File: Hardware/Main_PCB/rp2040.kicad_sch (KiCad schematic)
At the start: 27 parts, among them J3 Conn_02x18_Odd_Even, J4 Conn_02x18_Odd_Even, SW1 TL3342F160QG_TR, U3 RP2040, U3 W25Q128JVS, Y1 12Mhz

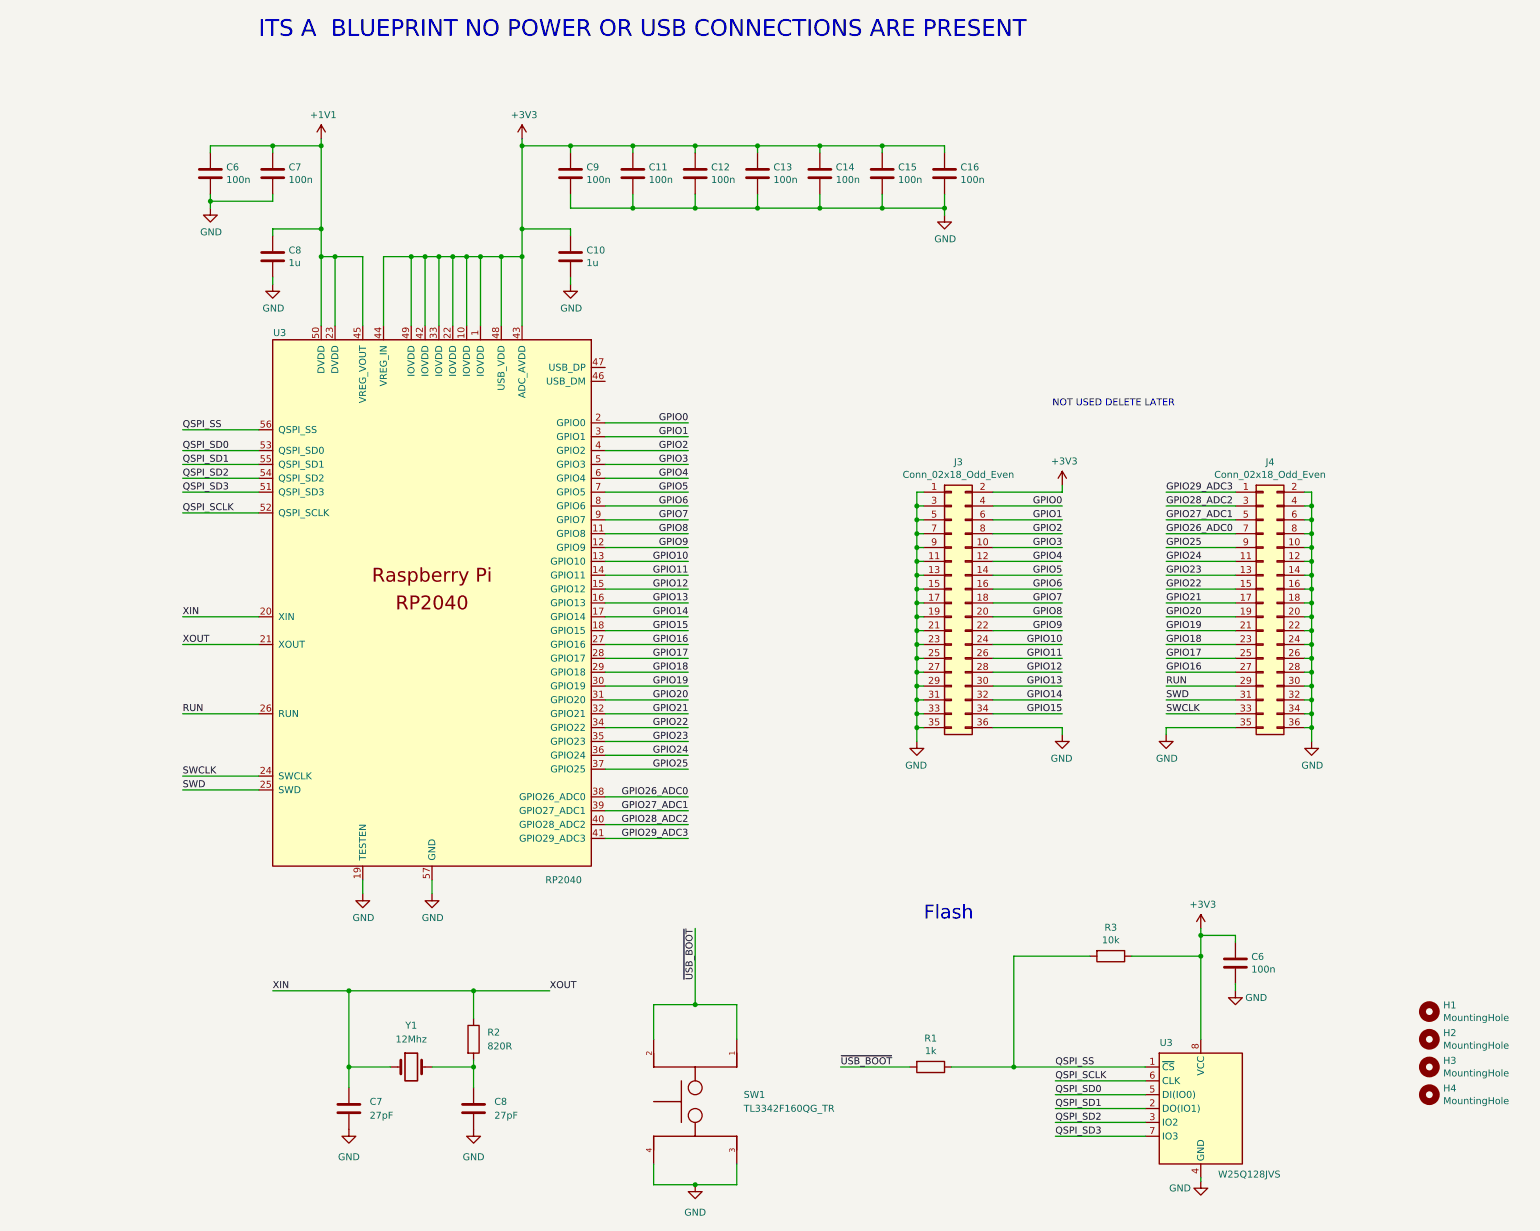
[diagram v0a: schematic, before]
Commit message: Trustworthy version of the MAIN PCB schematic
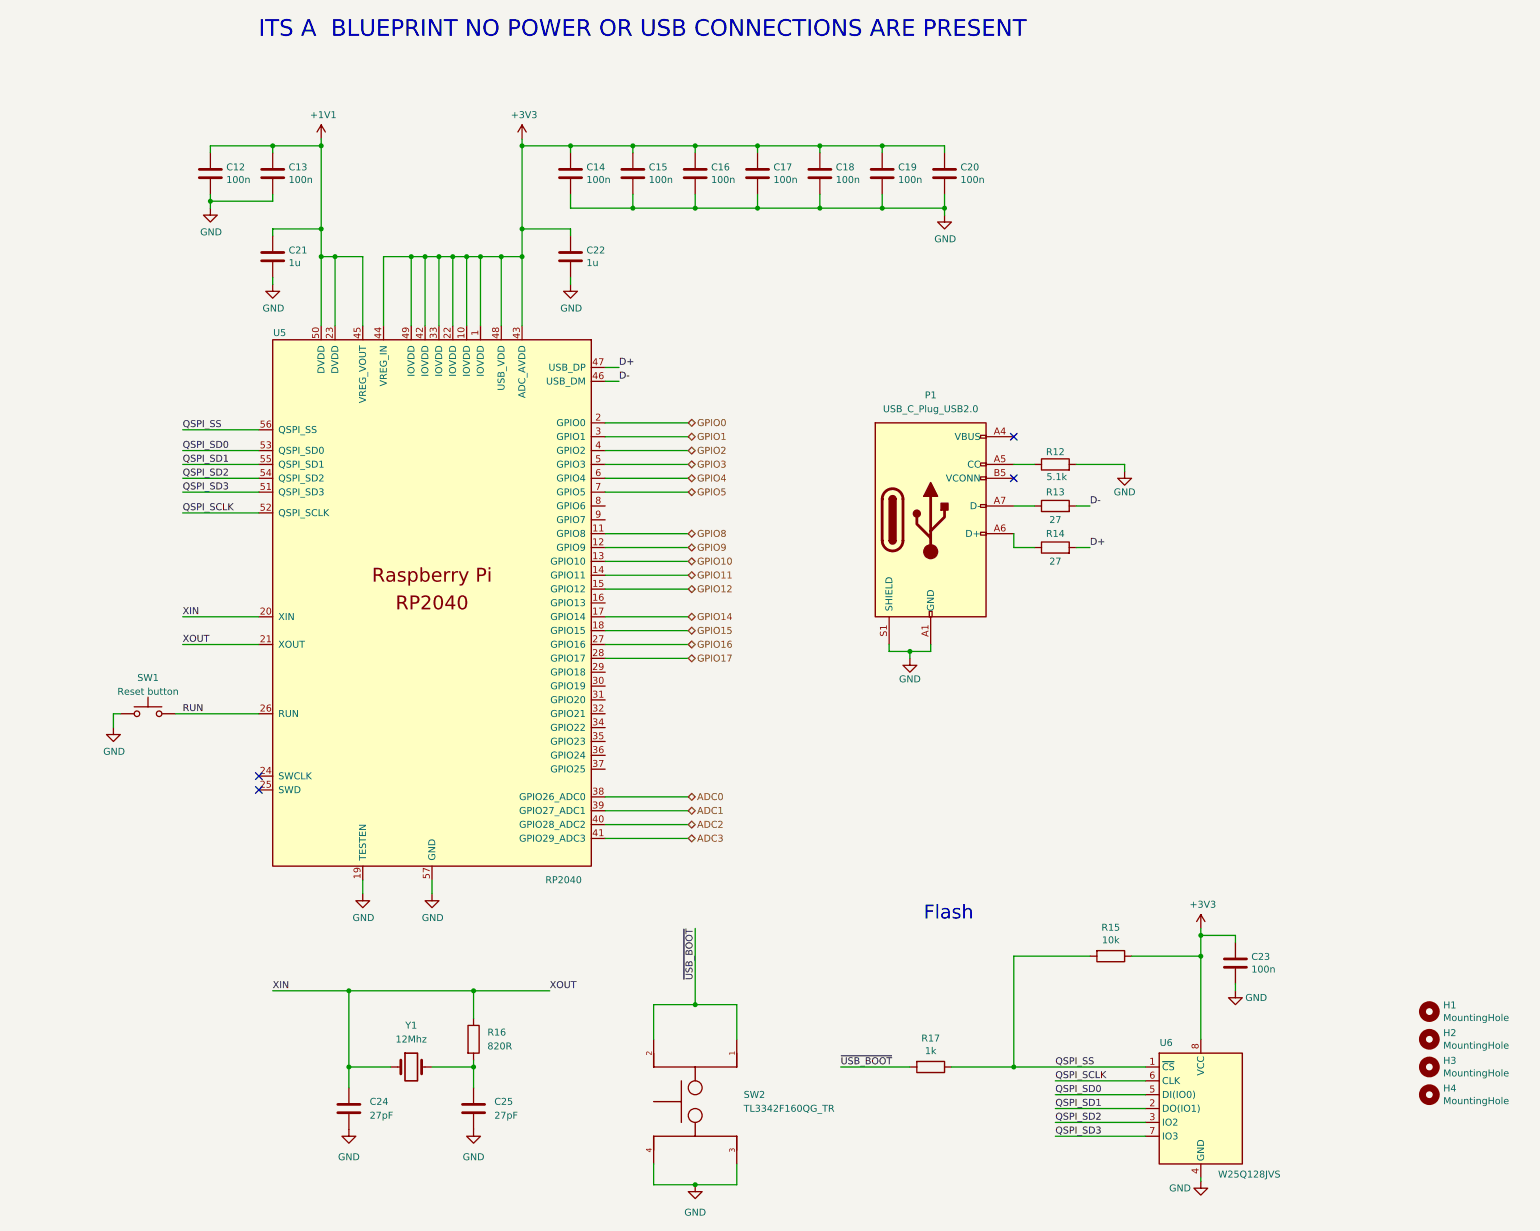
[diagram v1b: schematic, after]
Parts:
- removed J3, J4: Conn_02x18_Odd_Even, Connector_PinHeader_2.54mm:PinHeader_2x18_P2.54mm_Vertical, symbol Connector_Generic:Conn_02x18_Odd_Even
- added P1: USB_C_Plug_USB2.0, symbol Connector:USB_C_Plug_USB2.0
- added R12: 5.1k, symbol Device:R
- added R13, R14: 27, symbol Device:R
- added SW1: Reset button, symbol Switch:SW_Push
- renumbered C6 to C12, C7 to C13, C9 to C14, C11 to C15, C12 to C16, C13 to C17, C14 to C18, C15 to C19, C16 to C20, C8 to C21, C10 to C22, C6 to C23, C7 to C24, C8 to C25, R3 to R15, R2 to R16, R1 to R17, SW1 to SW2, U3 to U5, U3 to U6
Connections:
- net GND: now also P1.A1 (GND), P1.A12 (GND), P1.B1 (GND), P1.B12 (GND), P1.S1 (SHIELD), R12.2, SW1.1
- net RUN: now also SW1.2
- net D-: now reaches U5.46 (USB_DM)
- net D-: now also R13.2
- net D+: now reaches U5.47 (USB_DP)
- net D+: now also R14.2
- net GPIO13: no longer names the net of U5.16 (GPIO13)
- net GPIO18: no longer names the net of U5.29 (GPIO18)
- net GPIO19: no longer names the net of U5.30 (GPIO19)
- net GPIO20: no longer names the net of U5.31 (GPIO20)
- net GPIO21: no longer names the net of U5.32 (GPIO21)
- net GPIO22: no longer names the net of U5.34 (GPIO22)
- net GPIO23: no longer names the net of U5.35 (GPIO23)
- net GPIO24: no longer names the net of U5.36 (GPIO24)
- net GPIO25: no longer names the net of U5.37 (GPIO25)
- net GPIO26_ADC0 renamed ADC0
- net GPIO27_ADC1 renamed ADC1
- net GPIO28_ADC2 renamed ADC2
- net GPIO29_ADC3 renamed ADC3
- net GPIO6: no longer names the net of U5.8 (GPIO6)
- net GPIO7: no longer names the net of U5.9 (GPIO7)
- net SWCLK: no longer names the net of U5.24 (SWCLK)
- net SWD: no longer names the net of U5.25 (SWD)
- new net: P1.A7 (D-), R13.1
- new net: P1.A5 (CC), R12.1
- new net: P1.A4 (VBUS), P1.A9 (VBUS), P1.B4 (VBUS), P1.B9 (VBUS)
- new net: P1.A6 (D+), R14.1
- no-connect marks 0 -> 4
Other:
- note removed: "NOT USED DELETE LATER"

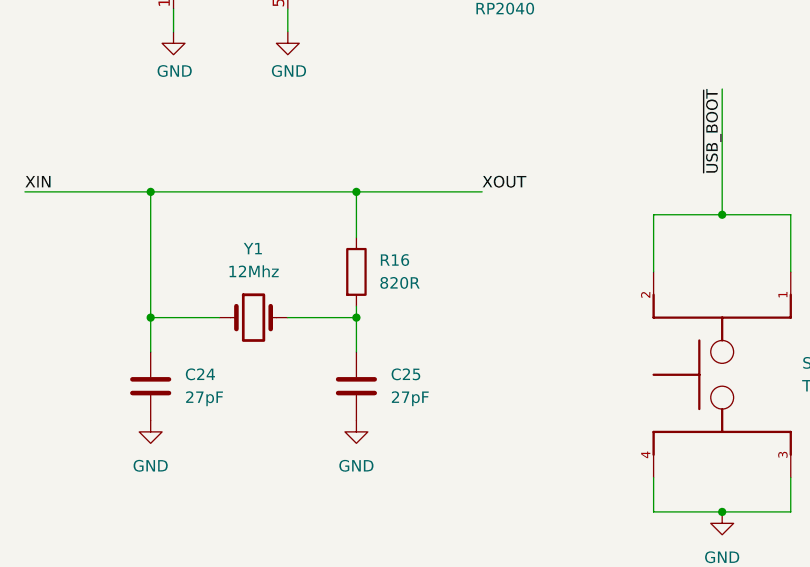
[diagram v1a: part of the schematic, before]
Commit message: Added some footprints
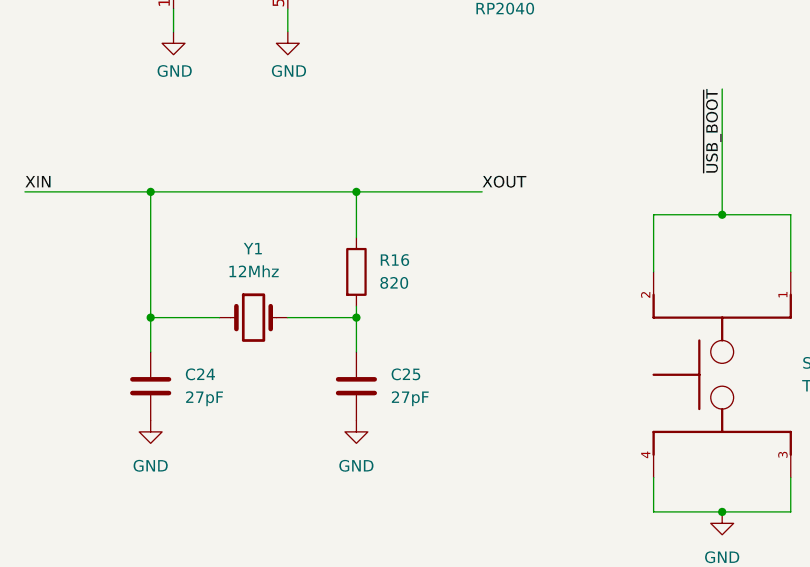
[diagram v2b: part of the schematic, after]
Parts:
- R16: value 820R -> 820
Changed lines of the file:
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@@
 			)
 		)
-		(property "Value" "820R"
+		(property "Value" "820"
 			(at 118.11 224.7899 0)
 			(effects

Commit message: Modifications to the MainPCB
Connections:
- net GPIO13: now reaches U5.16 (GPIO13)
- net GPIO18: now reaches U5.29 (GPIO18)
- net GPIO19: now reaches U5.30 (GPIO19)
- net GPIO6: now reaches U5.8 (GPIO6)
- net GPIO7: now reaches U5.9 (GPIO7)
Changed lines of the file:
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@@
+	(wire
+		(pts
+			(xy 139.7 158.75) (xy 154.94 158.75)
+		)
+		(stroke
+			(width 0)
+			(type default)
+		)
+	)
 	(wire
 		(pts
@@
 	(wire
 		(pts
+			(xy 139.7 125.73) (xy 154.94 125.73)
+		)
+		(stroke
+			(width 0)
+			(type default)
+		)
+	)
+	(wire
+		(pts
+			(xy 139.7 128.27) (xy 154.94 128.27)
+		)
+		(stroke
+			(width 0)
+			(type default)
+		)
+	)
+	(wire
+		(pts
 			(xy 214.63 125.73) (xy 218.44 125.73)
 		)
@@
 	(wire
 		(pts
+			(xy 139.7 143.51) (xy 154.94 143.51)
+		)
+		(stroke
+			(width 0)
+			(type default)
+		)
+	)
+	(wire
+		(pts
 			(xy 222.25 231.14) (xy 238.76 231.14)
 		)
@@
 		(pts
 			(xy 115.57 227.33) (xy 115.57 228.6)
+		)
+		(stroke
+			(width 0)
+			(type default)
+		)
+	)
+	(wire
+		(pts
+			(xy 139.7 156.21) (xy 154.94 156.21)
 		)
 		(stroke
@@
 		)
 	)
+	(hierarchical_label "GPIO6"
+		(shape bidirectional)
+		(at 154.94 125.73 0)
+		(effects
+			(font
+				(size 1.27 1.27)
+			)
+			(justify left)
+		)
+	)
 	(hierarchical_label "GPIO15"
 		(shape bidirectional)
@@
 		)
 	)
+	(hierarchical_label "GPIO19"
+		(shape bidirectional)
+		(at 154.94 158.75 0)
+		(effects
+			(font
+				(size 1.27 1.27)
+			)
+			(justify left)
+		)
+	)
+	(hierarchical_label "GPIO18"
+		(shape bidirectional)
+		(at 154.94 156.21 0)
+		(effects
+			(font
+				(size 1.27 1.27)
+			)
+			(justify left)
+		)
+	)
 	(hierarchical_label "GPIO14"
 		(shape bidirectional)
@@
 		)
 	)
+	(hierarchical_label "GPIO13"
+		(shape bidirectional)
+		(at 154.94 143.51 0)
+		(effects
+			(font
+				(size 1.27 1.27)
+			)
+			(justify left)
+		)
+	)
 	(hierarchical_label "GPIO3"
 		(shape bidirectional)
@@
 		(effects
 			(font
+				(size 1.27 1.27)
+			)
+			(justify left)
+		)
+	)
+	(hierarchical_label "GPIO7"
+		(shape bidirectional)
+		(at 154.94 128.27 0)
+		(effects
+			(font

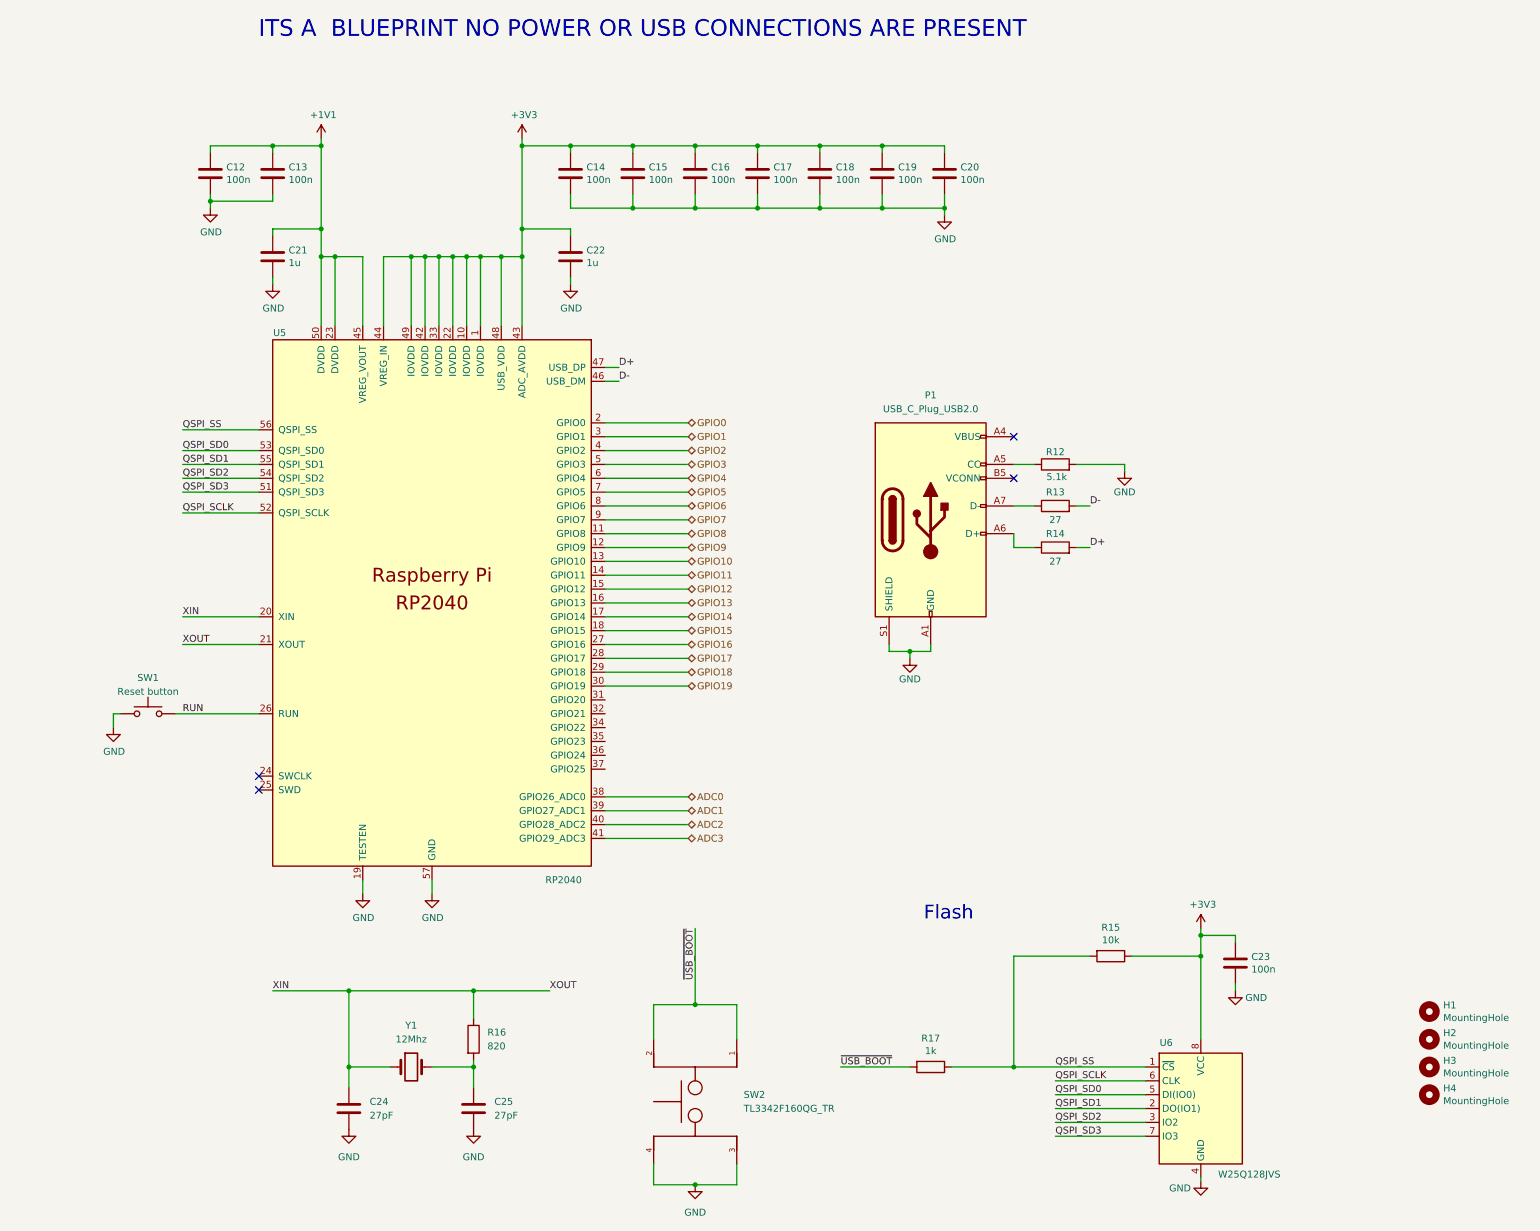
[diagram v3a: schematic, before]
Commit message: A finished version of the Main PCB schematic
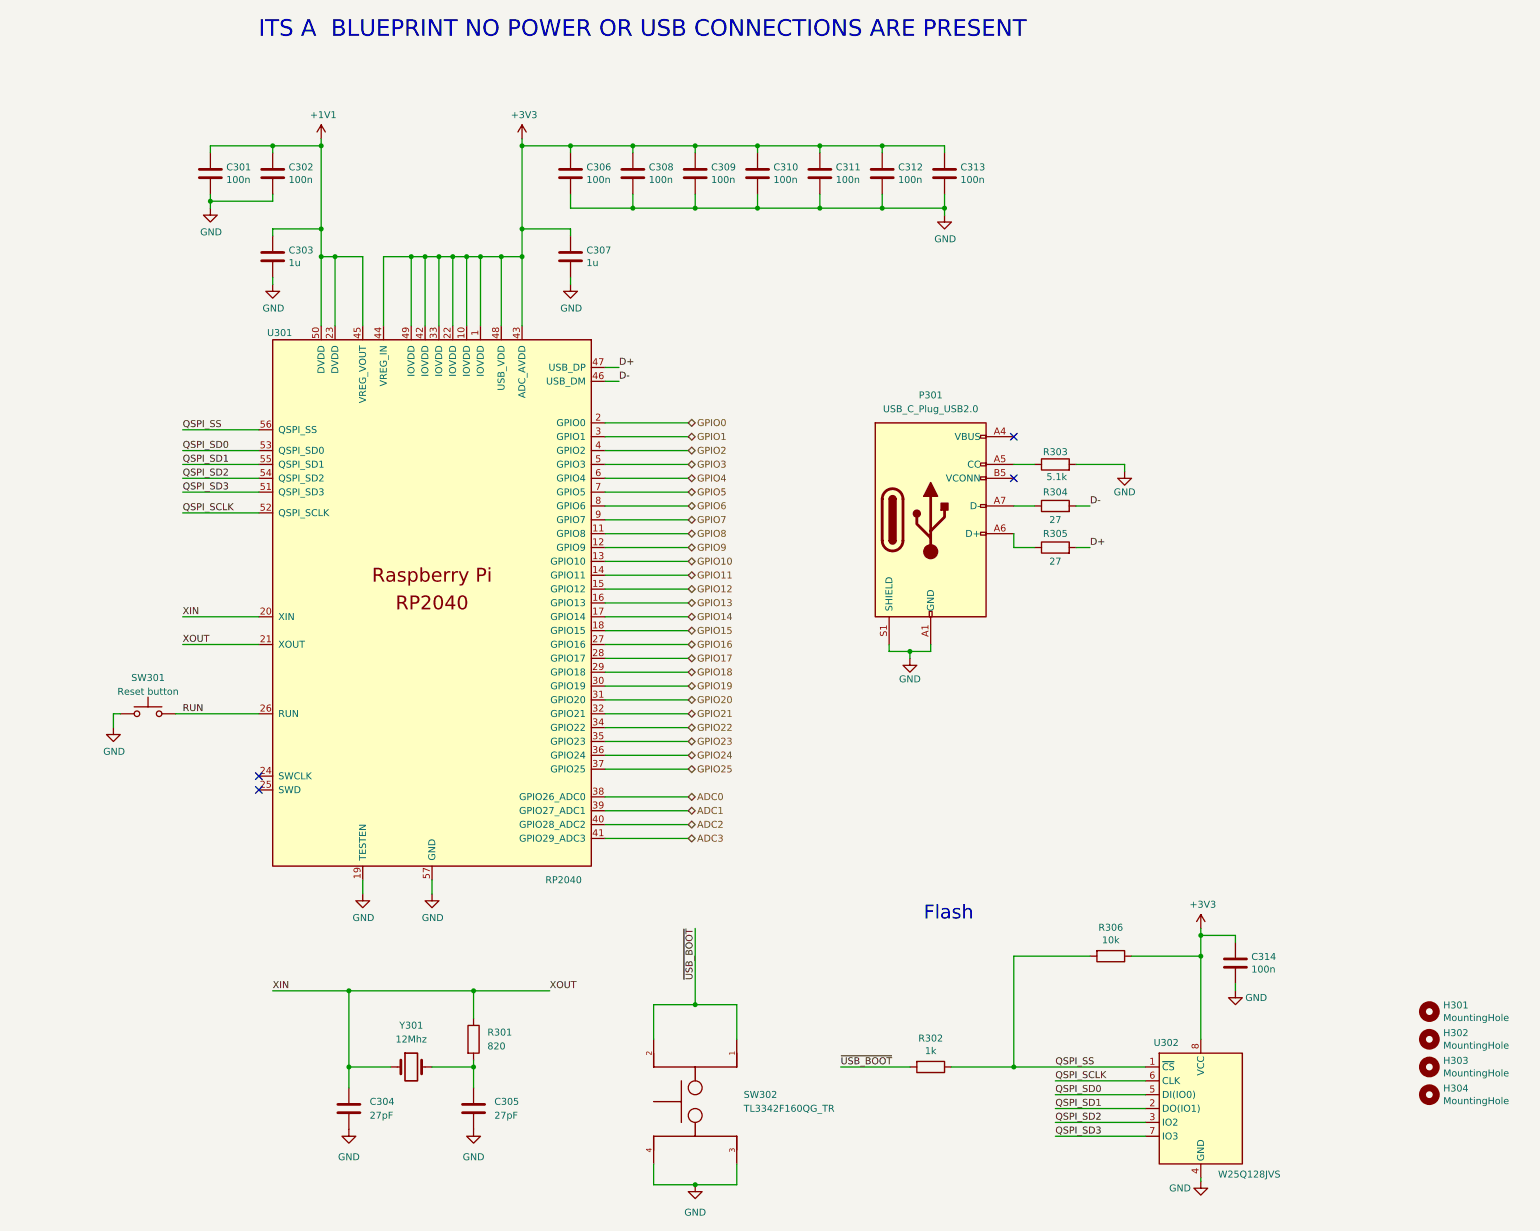
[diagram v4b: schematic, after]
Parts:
- renumbered C12 to C301, C13 to C302, C21 to C303, C24 to C304, C25 to C305, C14 to C306, C22 to C307, C15 to C308, C16 to C309, C17 to C310, C18 to C311, C19 to C312, C20 to C313, C23 to C314, H1 to H301, H2 to H302, H3 to H303, H4 to H304, P1 to P301, R16 to R301, R17 to R302, R12 to R303, R13 to R304, R14 to R305, R15 to R306, SW1 to SW301, SW2 to SW302, U5 to U301, U6 to U302, Y1 to Y301
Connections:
- net GPIO20: now reaches U301.31 (GPIO20)
- net GPIO21: now reaches U301.32 (GPIO21)
- net GPIO22: now reaches U301.34 (GPIO22)
- net GPIO23: now reaches U301.35 (GPIO23)
- net GPIO24: now reaches U301.36 (GPIO24)
- net GPIO25: now reaches U301.37 (GPIO25)
